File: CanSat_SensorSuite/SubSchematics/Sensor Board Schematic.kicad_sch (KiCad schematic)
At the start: 7 parts

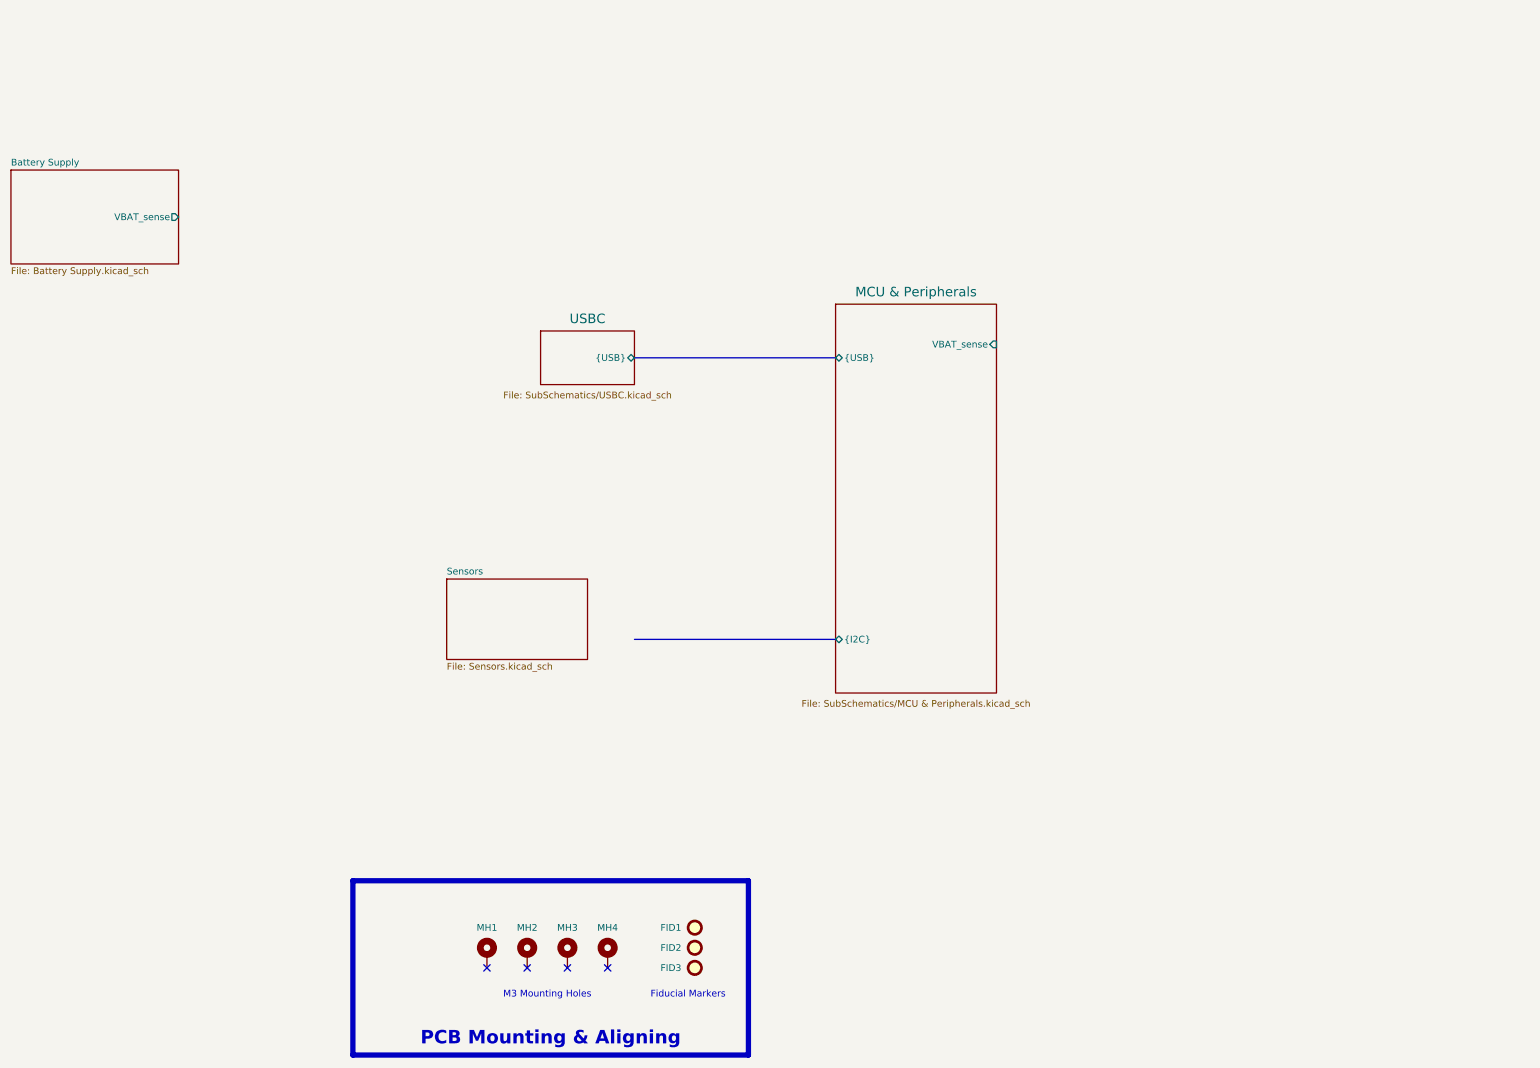
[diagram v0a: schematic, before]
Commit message: Minor schematic changes
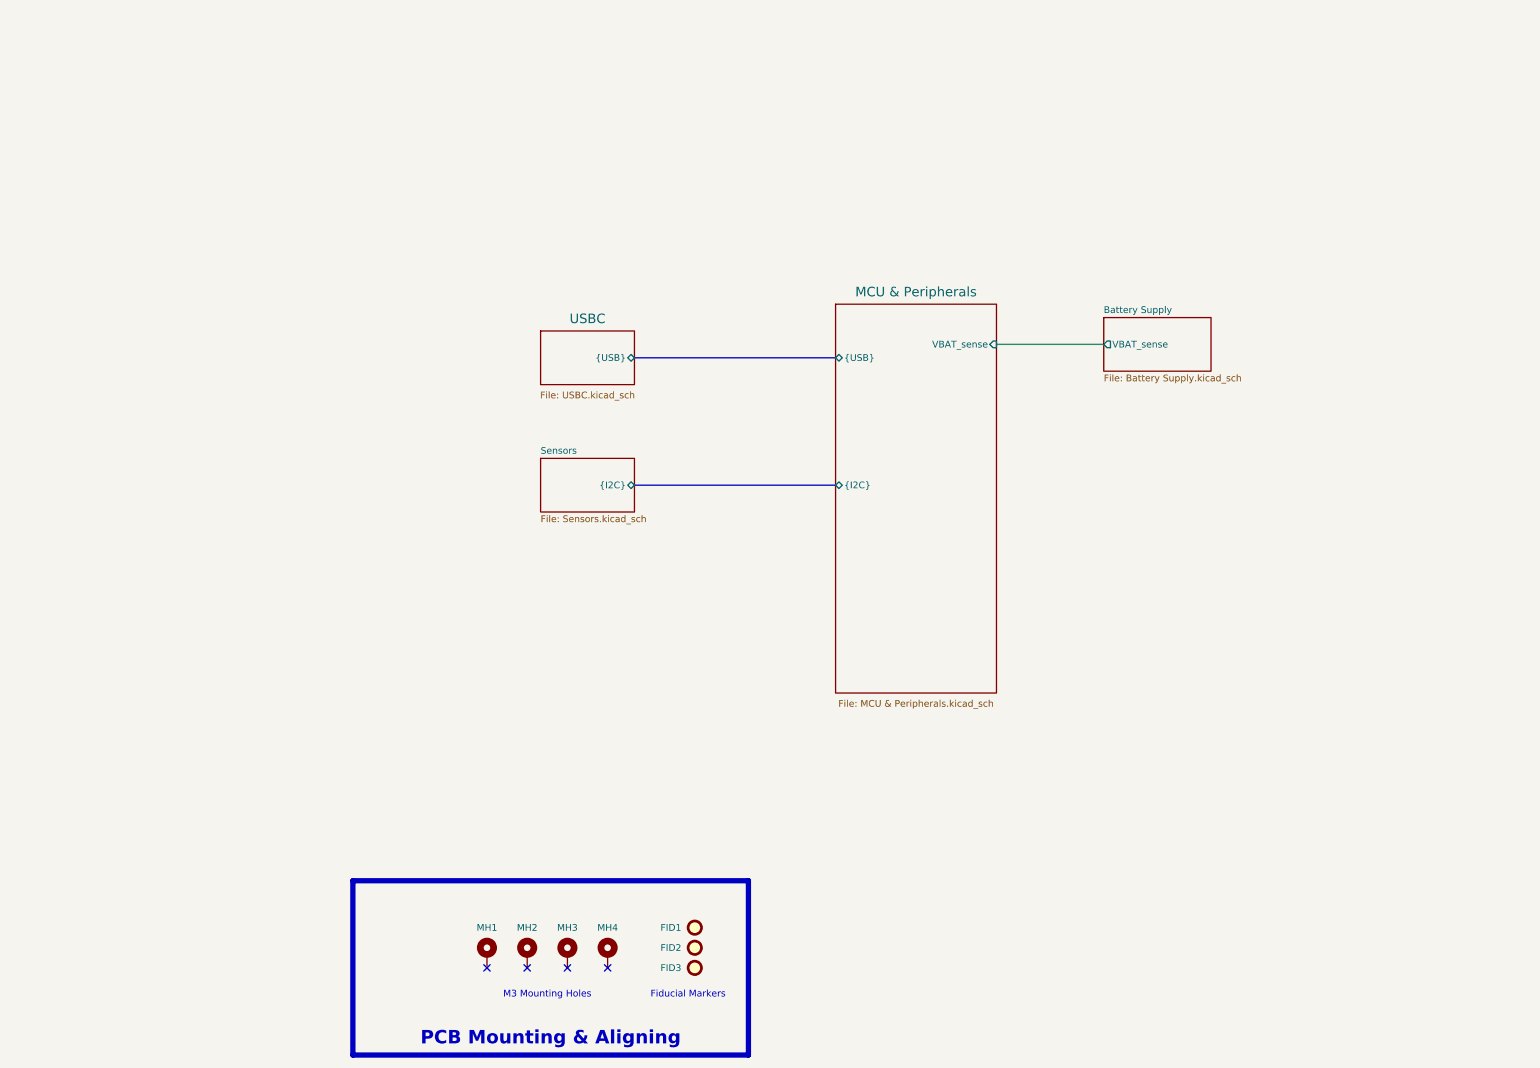
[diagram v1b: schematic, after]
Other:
- sheet MCU & Peripherals: file SubSchematics/MCU & Peripherals.kicad_sch -> MCU & Peripherals.kicad_sch
- sheet Sensors ports: added {I2C}; removed none
- sheet USBC: file SubSchematics/USBC.kicad_sch -> USBC.kicad_sch
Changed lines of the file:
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@@
 	(bus
 		(pts
-			(xy 175.26 137.16) (xy 213.36 137.16)
+			(xy 175.26 107.95) (xy 213.36 107.95)
+		)
+		(stroke
+			(width 0)
+			(type default)
+		)
+	)
+	(wire
+		(pts
+			(xy 243.84 81.28) (xy 264.16 81.28)
 		)
 		(stroke
@@
 	)
 	(sheet
-		(at 139.7 125.73)
-		(size 26.67 15.24)
+		(at 157.48 102.87)
+		(size 17.78 10.16)
 		(exclude_from_sim no)
 		(in_bom yes)
@@
 		)
 		(property "Sheetname" "Sensors"
-			(at 139.7 125.0184 0)
+			(at 157.48 102.1584 0)
 			(effects
 				(font
@@
 		)
 		(property "Sheetfile" "Sensors.kicad_sch"
-			(at 139.7 141.5546 0)
+			(at 157.48 113.6146 0)
 			(effects
 				(font
@@
 				)
 				(justify left top)
+			)
+		)
+		(pin "{I2C}" bidirectional
+			(at 175.26 107.95 0)
+			(effects
+				(font
+					(size 1.27 1.27)
+				)
+				(justify right)
 			)
 		)
@@
 			)
 		)
-		(property "Sheetfile" "SubSchematics/USBC.kicad_sch"
+		(property "Sheetfile" "USBC.kicad_sch"
 			(at 166.37 90.17 0)
 			(effects
@@
 			)
 		)
-		(property "Sheetfile" "SubSchematics/MCU & Peripherals.kicad_sch"
+		(property "Sheetfile" "MCU & Peripherals.kicad_sch"
 			(at 228.6 148.59 0)
 			(effects
@@
 		)
 		(pin "{I2C}" bidirectional
-			(at 213.36 137.16 180)
+			(at 213.36 107.95 180)
 			(effects
 				(font
@@
 	)
 	(sheet
-		(at 57.15 48.26)
-		(size 31.75 17.78)
+		(at 264.16 76.2)
+		(size 20.32 10.16)
 		(exclude_from_sim no)
 		(in_bom yes)
@@
 		)
 		(property "Sheetname" "Battery Supply"
-			(at 57.15 47.5484 0)
+			(at 264.16 75.4884 0)
 			(effects
 				(font
@@
 		)
 		(property "Sheetfile" "Battery Supply.kicad_sch"
-			(at 57.15 66.6246 0)
+			(at 264.16 86.9446 0)
 			(effects
 				(font
@@
 		)
 		(pin "VBAT_sense" output
-			(at 88.9 57.15 0)
-			(effects
-				(font
-					(size 1.27 1.27)
-				)
-				(justify right)
-			)
-		)
+			(at 264.16 81.28 180)
+			(effects
+				(font
+					(size 1.27 1.27)
+				)
+				(justify left)
+			)
+		)

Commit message: Example files update
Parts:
- renumbered FID1 to FID301, FID2 to FID302, FID3 to FID303, MH1 to MH301, MH2 to MH302, MH3 to MH303, MH4 to MH304
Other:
- sheet Sensors renamed AtmoSensors
- added sheet PosSensors (PosSensors.kicad_sch)
- sheet AtmoSensors: file Sensors.kicad_sch -> AtmoSensors.kicad_sch
- company: (none) -> ${COMPANY}
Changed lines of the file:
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@@
 	(generator_version "9.0")
 	(paper "A3")
+	(title_block
+		(date "2026-01-04")
+		(rev "${REVISION}")
+		(company "${COMPANY}")
+		(comment 1 "GRID - mil (1.27mm, 2.54mm)")
+	)
 	(rectangle
 		(start 121.92 182.88)
@@
 		)
 	)
+	(junction
+		(at 194.31 107.95)
+		(diameter 0)
+		(color 0 0 0 0)
+	)
 	(no_connect
 		(at 162.56 199.39)
@@
 	(bus
 		(pts
-			(xy 175.26 107.95) (xy 213.36 107.95)
+			(xy 175.26 107.95) (xy 194.31 107.95)
 		)
 		(stroke
@@
 		)
 	)
+	(bus
+		(pts
+			(xy 194.31 107.95) (xy 213.36 107.95)
+		)
+		(stroke
+			(width 0)
+			(type default)
+		)
+	)
+	(bus
+		(pts
+			(xy 175.26 134.62) (xy 194.31 134.62)
+		)
+		(stroke
+			(width 0)
+			(type default)
+		)
+	)
+	(bus
+		(pts
+			(xy 194.31 134.62) (xy 194.31 107.95)
+		)
+		(stroke
+			(width 0)
+			(type default)
+		)
+	)
 	(wire
 		(pts
-			(xy 243.84 81.28) (xy 264.16 81.28)
+			(xy 243.84 83.82) (xy 264.16 83.82)
 		)
 		(stroke
@@
 		(on_board yes)
 		(dnp no)
-		(property "Reference" "MH3"
+		(property "Reference" "MH303"
 			(at 162.56 191.77 0)
 			(effects
@@
 			(project "CanSat_SensorSuite"
 				(path "/0650c7a8-acba-429c-9f8e-eec0baf0bc1c/459e6a54-4354-4cbe-b679-1f9dcd1ee4fd"
-					(reference "MH3")
+					(reference "MH303")
 					(unit 1)
 				)
@@
 		(on_board yes)
 		(dnp no)
-		(property "Reference" "FID1"
+		(property "Reference" "FID301"
 			(at 184.15 191.77 0)
 			(effects
@@
 			(project "CanSat_SensorSuite"
 				(path "/0650c7a8-acba-429c-9f8e-eec0baf0bc1c/459e6a54-4354-4cbe-b679-1f9dcd1ee4fd"
-					(reference "FID1")
+					(reference "FID301")
 					(unit 1)
 				)
@@
 		(on_board yes)
 		(dnp no)
-		(property "Reference" "FID3"
+		(property "Reference" "FID303"
 			(at 184.15 199.39 0)
 			(effects
@@
 			(project "CanSat_SensorSuite"
 				(path "/0650c7a8-acba-429c-9f8e-eec0baf0bc1c/459e6a54-4354-4cbe-b679-1f9dcd1ee4fd"
-					(reference "FID3")
+					(reference "FID303")
 					(unit 1)
 				)
@@
 		(on_board yes)
 		(dnp no)
-		(property "Reference" "MH4"
+		(property "Reference" "MH304"
 			(at 170.18 191.77 0)
 			(effects
@@
 			(project "CanSat_SensorSuite"
 				(path "/0650c7a8-acba-429c-9f8e-eec0baf0bc1c/459e6a54-4354-4cbe-b679-1f9dcd1ee4fd"
-					(reference "MH4")
+					(reference "MH304")
 					(unit 1)
 				)
@@
 		(on_board yes)
 		(dnp no)
-		(property "Reference" "MH1"
+		(property "Reference" "MH301"
 			(at 147.32 191.77 0)
 			(effects
@@
 			(project "CanSat_SensorSuite"
 				(path "/0650c7a8-acba-429c-9f8e-eec0baf0bc1c/459e6a54-4354-4cbe-b679-1f9dcd1ee4fd"
-					(reference "MH1")
+					(reference "MH301")
 					(unit 1)
 				)
@@
 		(on_board yes)
 		(dnp no)
-		(property "Reference" "FID2"
+		(property "Reference" "FID302"
 			(at 184.15 195.58 0)
 			(effects
@@
 			(project "CanSat_SensorSuite"
 				(path "/0650c7a8-acba-429c-9f8e-eec0baf0bc1c/459e6a54-4354-4cbe-b679-1f9dcd1ee4fd"
-					(reference "FID2")
+					(reference "FID302")
 					(unit 1)
 				)
@@
 		(on_board yes)
 		(dnp no)
-		(property "Reference" "MH2"
+		(property "Reference" "MH302"
 			(at 154.94 191.77 0)
 			(effects
@@
 			(project "CanSat_SensorSuite"
 				(path "/0650c7a8-acba-429c-9f8e-eec0baf0bc1c/459e6a54-4354-4cbe-b679-1f9dcd1ee4fd"
-					(reference "MH2")
+					(reference "MH302")
 					(unit 1)
 				)
@@
 		(on_board yes)
 		(dnp no)
-		(fields_autoplaced yes)
 		(stroke
 			(width 0.1524)
@@
 			(color 101 130 255 1.0000)
 		)
-		(property "Sheetname" "Sensors"
-			(at 157.48 102.1584 0)
-			(effects
-				(font
-					(size 1.27 1.27)
-				)
-				(justify left bottom)
-			)
-		)
-		(property "Sheetfile" "Sensors.kicad_sch"
-			(at 157.48 113.6146 0)
-			(effects
-				(font
-					(size 1.27 1.27)
-				)
-				(justify left top)
+		(property "Sheetname" "AtmoSensors"
+			(at 166.37 101.6 0)
+			(effects
+				(font
+					(size 1.8 1.8)
+				)
+				(justify bottom)
+			)
+		)
+		(property "Sheetfile" "AtmoSensors.kicad_sch"
+			(at 166.37 114.3 0)
+			(effects
+				(font
+					(size 1.27 1.27)
+				)
+				(justify top)
 			)
 		)
@@
 		)
 		(pin "VBAT_sense" input
-			(at 243.84 81.28 0)
+			(at 243.84 83.82 0)
 			(effects
 				(font
@@
 	)
 	(sheet
-		(at 264.16 76.2)
+		(at 264.16 78.74)
 		(size 20.32 10.16)
 		(exclude_from_sim no)
@@
 		)
 		(property "Sheetname" "Battery Supply"
-			(at 264.16 75.4884 0)
+			(at 264.16 78.0284 0)
 			(effects
 				(font
@@
 		)
 		(property "Sheetfile" "Battery Supply.kicad_sch"
-			(at 264.16 86.9446 0)
+			(at 264.16 89.4846 0)
 			(effects
 				(font
@@
 		)
 		(pin "VBAT_sense" output
-			(at 264.16 81.28 180)
+			(at 264.16 83.82 180)
 			(effects
 				(font
@@
 				)
 			)
+		)
+	)
+	(sheet
+		(at 157.48 129.54)
+		(size 17.78 10.16)
+		(exclude_from_sim no)
+		(in_bom yes)
+		(on_board yes)
+		(dnp no)
+		(stroke
+			(width 0.1524)
+			(type solid)
+		)
+		(fill
+			(color 101 130 255 1.0000)
+		)
+		(property "Sheetname" "PosSensors"
+			(at 166.37 128.27 0)
+			(effects
+				(font
+					(size 1.8 1.8)
+				)
+				(justify bottom)
+			)
+		)
+		(property "Sheetfile" "PosSensors.kicad_sch"
+			(at 166.37 140.97 0)
+			(effects
+				(font
+					(size 1.27 1.27)
+				)
+				(justify top)
+			)
+		)
+		(pin "{I2C}" bidirectional
+			(at 175.26 134.62 0)
+			(effects
+				(font
+					(size 1.27 1.27)
+				)
+				(justify right)
+			)
+		)
+		(instances
+			(project "CanSat_SensorSuite"
+				(path "/0650c7a8-acba-429c-9f8e-eec0baf0bc1c/459e6a54-4354-4cbe-b679-1f9dcd1ee4fd"
+					(page "8")
+				)
+			)

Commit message: Major sensor suite board changes, start of PCB layout
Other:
- sheet Battery Supply renamed USBC & Battery Supply
- removed sheet USBC
- sheet USBC & Battery Supply: file Battery Supply.kicad_sch -> USBC_Battery Supply.kicad_sch
- sheet USBC & Battery Supply ports: added {USB}; removed none
- title: (none) -> Sensor Suite Board Overview
- moved on the sheet: FID301, FID302, FID303, MH301, MH302, MH303, MH304
